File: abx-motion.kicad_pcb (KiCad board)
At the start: 4 copper layers, 157 x 105 mm, 252 parts, among them J1 XT60_BAT, J102 E_STOP, J201 USB-C, J202 ENC1_CONN, J203 ENC2_CONN, J204 CAN_TERM, J205 CAN_BUS, J206 RS485_TERM, J207 RS485_BUS, J208 OLED_I2C, J209 I2C_EXP, J301 MOTOR_OUT, J401 MOTOR_OUT, J501 STEP1_MOTOR, J502 STEP1_EXT, J503 STEP2_MOTOR, J504 STEP2_EXT, J505 RELAY1_OUT, J506 RELAY2_OUT, J601 B3B-PH-K-S, J602 B3B-PH-K-S, J603 B3B-PH-K-S, J604 B3B-PH-K-S, J605 B3B-PH-K-S, J606 B3B-PH-K-S, K501 G5LE-14-DC5, K502 G5LE-14-DC5, Q1 SQJ459EP-T1_GE3, Q301 CSD18540Q5B, Q302 CSD18540Q5B, Q303 CSD18540Q5B, Q304 CSD18540Q5B, Q401 CSD18540Q5B, Q402 CSD18540Q5B, Q403 CSD18540Q5B, Q404 CSD18540Q5B, Q501 AO3400A, Q502 AO3400A, Q503 AO3400A, Q504 AO3400A, Q601 AO3400A, Q602 AO3400A, SW201 RESET, SW202 BOOT, SW203 BTN_BACK, SW204 BTN_NEXT, SW205 BTN_HOME, SW501 MICROSTEP_CFG, SW502 MICROSTEP_CFG, U1 LMR36520FADDA, U2 AP2112K-3.3, U201 USBLC6-2SC6, U202 TCAN1042V-Q1, U203 THVD1450DR, U3 ESP32-S3-WROOM-1-N8R2, U301 DRV8701ERGER, U4 74LVC14A, U401 DRV8701ERGER, U501 StepStick_DRV8825, U502 StepStick_DRV8825, U601 PCA9555PW,118

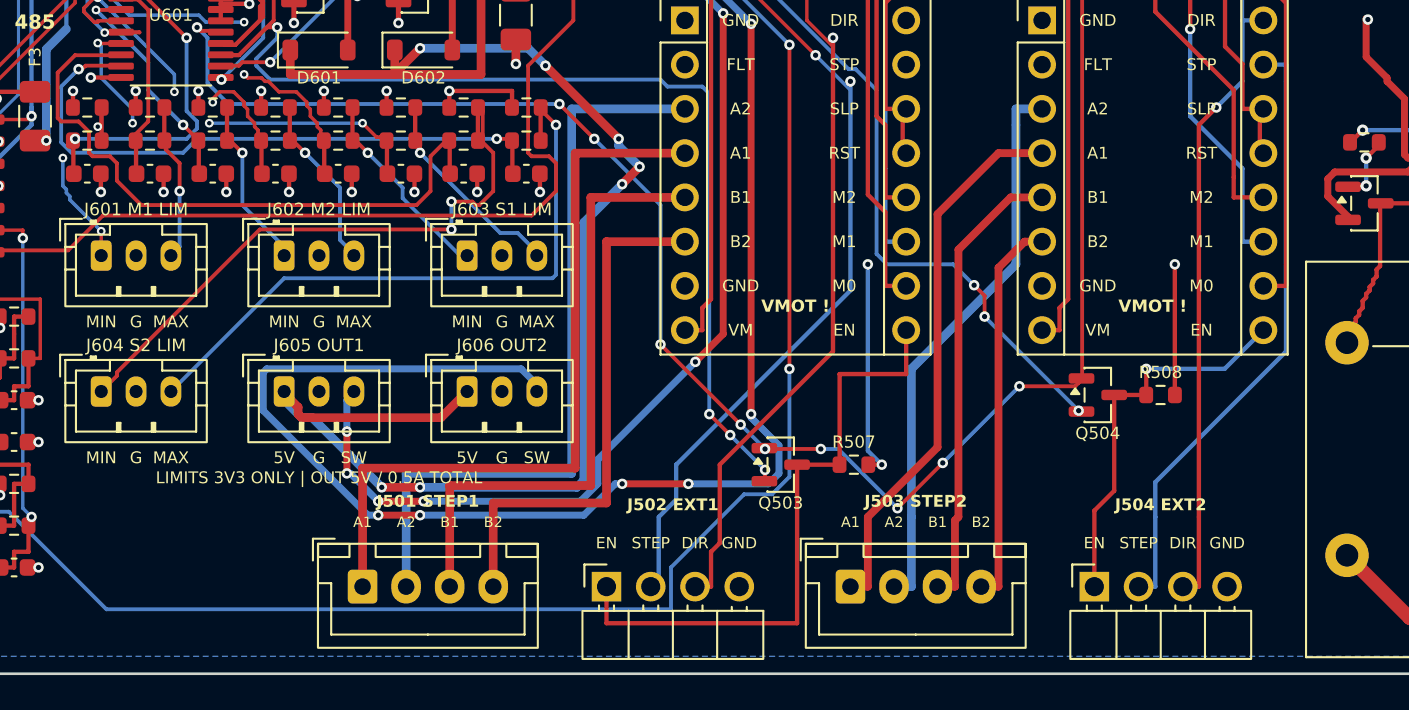
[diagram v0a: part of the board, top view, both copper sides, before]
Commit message: Pack upright EXT headers and symmetric motor connectors to the right
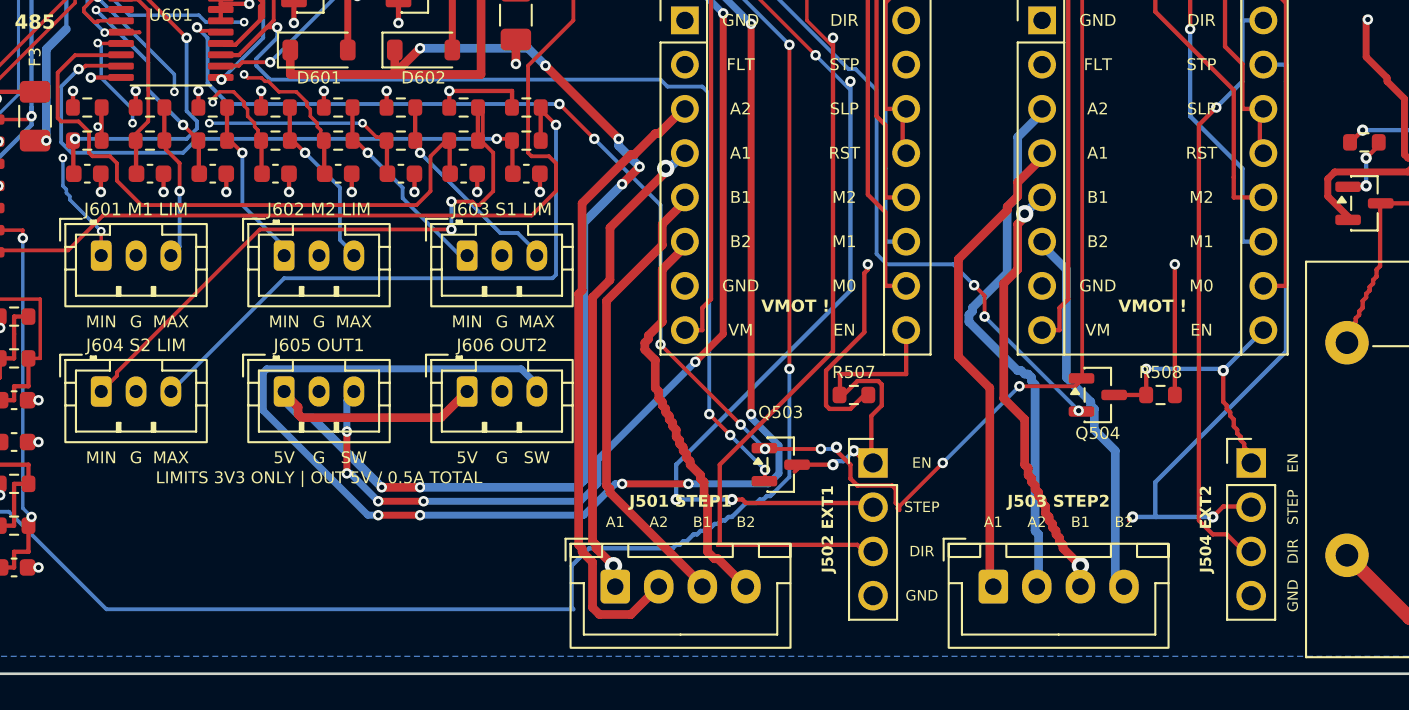
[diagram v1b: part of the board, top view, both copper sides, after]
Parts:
- J502, J504: footprint abx-footprints:EXT_Header_1x04_P2.54mm_RightAngle -> abx-footprints:EXT_Header_1x04_P2.54mm_Vertical
- moved J502 16.9 mm to (111.3, 140.9), turned to 0 degrees
- moved J501 14.5 mm to (96.5, 148.0)
- moved J504 11.5 mm to (133.0, 140.9), turned to 0 degrees
- moved J503 8.20 mm to (118.2, 148.0)
- moved R507 4.00 mm to (110.2, 137.0)
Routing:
- net /Steppers_and_Relays/STEP1_A1: track 43.4 -> 27.8 mm, vias 0 -> 2
- net /Steppers_and_Relays/STEP1_EN_GATED: track 36.1 -> 20.7 mm, vias 0 -> 2
- net /Steppers_and_Relays/STEP1_B1: track 35.8 -> 26.8 mm
- net /Steppers_and_Relays/STEP1_B2: track 30.8 -> 23.3 mm
- net /Steppers_and_Relays/STEP1_A2: track 43.4 -> 36.4 mm
- net /STEP1_PUL: track 90.0 -> 95.7 mm, vias 2 -> 4
- net /STEP1_DIR: track 94.9 -> 100.6 mm
- net /Steppers_and_Relays/STEP2_EN_GATED: track 22.5 -> 17.1 mm, vias 1 -> 2
- net /Steppers_and_Relays/STEP2_A1: track 31.5 -> 27.7 mm
- net /STEP2_PUL: track 96.8 -> 99.3 mm, vias 1 -> 3
- net /+3V3_DRV_EN: track 267.9 -> 269.6 mm
- net /Steppers_and_Relays/STEP2_B1: track 26.5 -> 25.2 mm, vias 0 -> 2
- net /Steppers_and_Relays/STEP2_A2: track 32.4 -> 31.2 mm
- net /STEP2_DIR: track 91.3 -> 90.3 mm
- net +3V3: track 310.5 -> 309.8 mm, vias 49 -> 48
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
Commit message: Pack digital I/O beneath OLED and straighten local routing
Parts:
- J208: footprint Connector_PinSocket_2.54mm:PinSocket_1x04_P2.54mm_Vertical -> abx-footprints:OLED_Socket_SLW_1x04_P2.54mm_LowProfile
- moved Q601 24.5 mm to (80.0, 89.0)
- moved Q602 24.5 mm to (85.5, 89.0)
- moved D601 24.2 mm to (80.5, 93.0)
- moved D602 24.2 mm to (86.0, 93.0)
- moved F5 24.2 mm to (90.5, 91.0)
- moved U601 23.7 mm to (71.5, 91.5)
- moved R601 23.4 mm to (67.5, 97.1)
- moved R609 23.4 mm to (67.5, 99.0)
- moved C602 23.4 mm to (67.5, 100.9)
- moved R602 23.4 mm to (70.9, 97.1)
- moved R610 23.4 mm to (70.9, 99.0)
- moved C603 23.4 mm to (70.9, 100.9)
- moved R603 23.4 mm to (74.3, 97.1)
- moved R611 23.4 mm to (74.3, 99.0)
- moved C604 23.4 mm to (74.3, 100.9)
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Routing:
- net /Industrial_IO/OUT2_SW: track 101.5 -> 51.9 mm, vias 7 -> 3
- net /+3V3_DRV_EN: track 269.6 -> 297.6 mm, vias 18 -> 22
- net /Industrial_IO/OUT1_SW: track 77.4 -> 51.2 mm, vias 7 -> 5
- net +5V: track 170.7 -> 195.8 mm, vias 21 -> 22
- net /Industrial_IO/S1_MIN_RAW: track 11.6 -> 36.0 mm
- net /Industrial_IO/S1_MAX_RAW: track 12.1 -> 35.1 mm
- net /STEP2_EN: track 82.7 -> 103.6 mm, vias 4 -> 10
- net +3V3: track 309.8 -> 330.3 mm, vias 48 -> 49
- net /IO_INT_N: track 75.7 -> 57.9 mm, vias 2 -> 6
- net /I2C_SCL: track 143.7 -> 128.4 mm, vias 7 -> 8
- net /Industrial_IO/+5V_OUT: track 89.6 -> 74.7 mm, vias 7 -> 3
- net /MCU_and_Encoders/ENC1_A: track 84.6 -> 99.1 mm, vias 2 -> 9
- net /Industrial_IO/M2_MAX_IN: track 20.3 -> 34.7 mm, vias 3 -> 4
- net /STEP1_EN: track 72.7 -> 86.6 mm, vias 4 -> 9
- net /Industrial_IO/S1_MAX_IN: track 24.2 -> 35.4 mm, vias 4 -> 3
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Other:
- board text added: "LIMITS 3V3 | OUT 5V / 0.5A TOTAL"
- board text added: "OLED - 10 mm STANDOFFS"
- board text removed: "0.96 / 1.3 OLED MODULE"
- board text removed: "LIMITS 3V3 ONLY | OUT 5V / 0.5A TOTAL"
